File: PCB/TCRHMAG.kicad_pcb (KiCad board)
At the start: 2 copper layers, 45 x 36.1 mm, 12 parts, among them J1 CONN_BATTERY, J2 CONN_LED, J3 CONN_THERM, SW1 PWR_SW, U1 CH32V003FxPx, U2 L78L05_SOT89

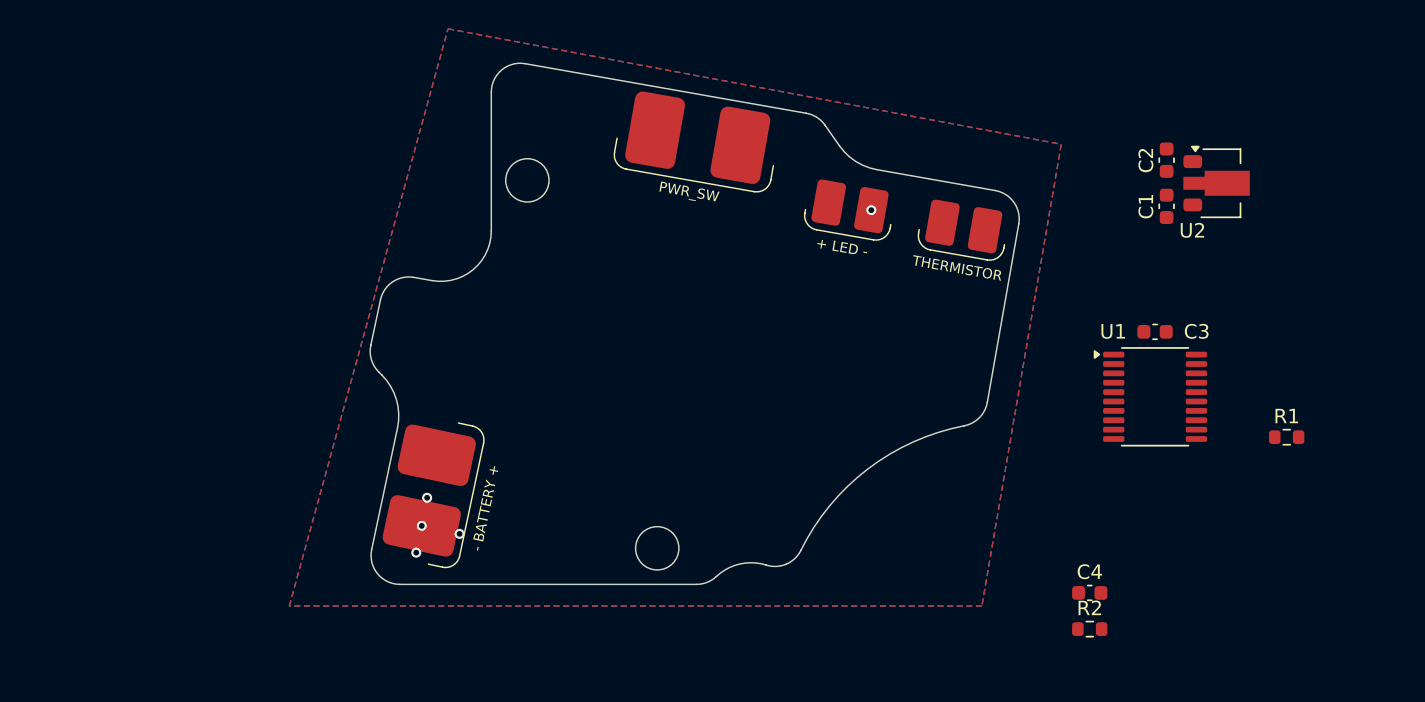
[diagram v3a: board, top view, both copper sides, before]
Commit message: Added High Current and MCU to PCB
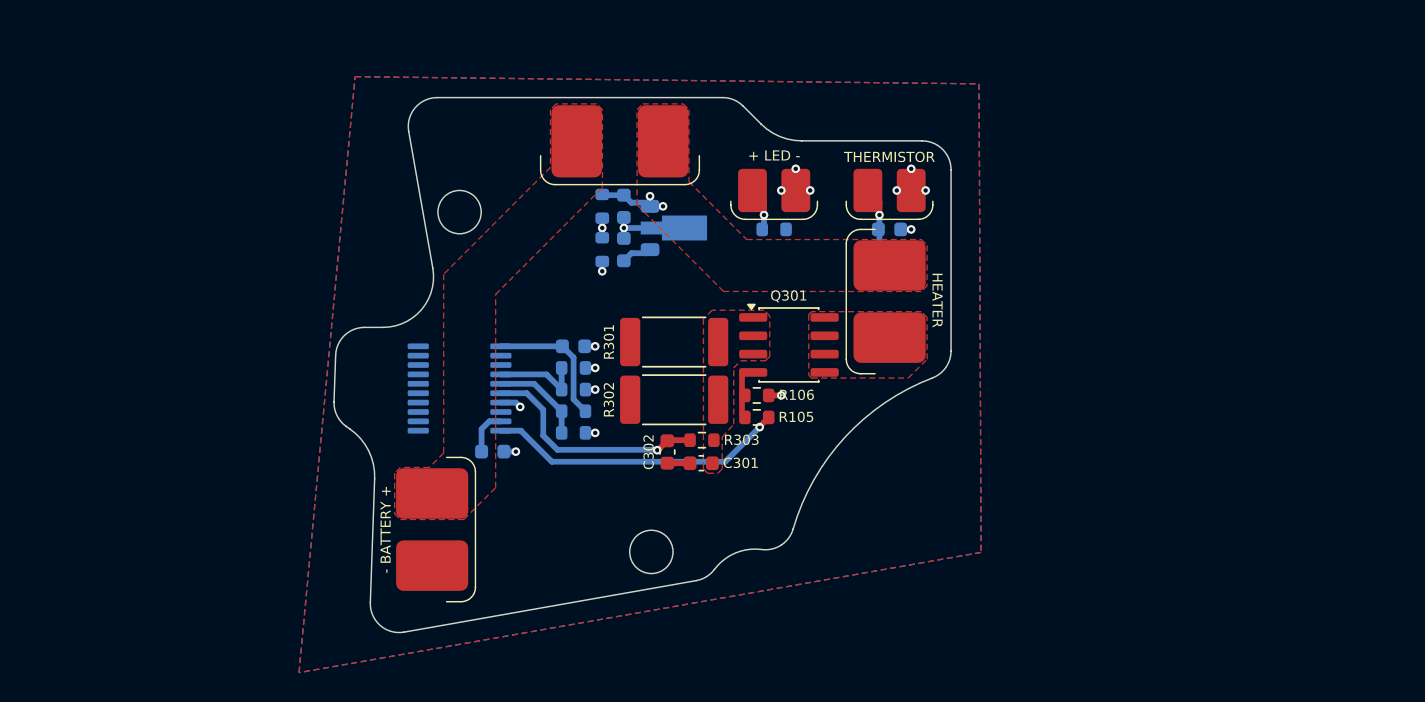
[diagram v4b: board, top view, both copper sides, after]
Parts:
- removed C1, C3: 100nF, Capacitor_SMD:C_0603_1608Metric
- removed C2: 10uF, Capacitor_SMD:C_0603_1608Metric
- removed C4: 1uF, Capacitor_SMD:C_0603_1608Metric
- removed R1: 330R, Resistor_SMD:R_0603_1608Metric
- removed R2: 4K7, Resistor_SMD:R_0603_1608Metric
- removed SW1: PWR_SW, TCRHMAG:U13SS_Switch
- removed U1: CH32V003FxPx, Package_SO:TSSOP-20_4.4x6.5mm_P0.65mm
- removed U2: L78L05_SOT89, Package_TO_SOT_SMD:SOT-89-3
- added C101: 100nF, Capacitor_SMD:C_0603_1608Metric, B.Cu at (82.7, 63.8)
- added C102: 10uF, Capacitor_SMD:C_0603_1608Metric, B.Cu at (82.7, 66.8)
- added C103: 1uF, Capacitor_SMD:C_0603_1608Metric, B.Cu at (101.1, 65.4)
- added C104: 100nF, Capacitor_SMD:C_0603_1608Metric, B.Cu at (73.6, 80.8)
- added C201: 100nF, Capacitor_SMD:C_0603_1608Metric, B.Cu at (79.2, 73.5)
- added C301: 100nF, Capacitor_SMD:C_0603_1608Metric, F.Cu at (88.0, 81.6)
- added C302: 100nF, Capacitor_SMD:C_0603_1608Metric, F.Cu at (85.7, 80.8)
- added J5: CONN_HEATER, TCRHMAG:Power_Conn, F.Cu at (101.1, 70.4)
- added Q301: Si4116DY, Package_SO:SOIC-8_3.9x4.9mm_P1.27mm, F.Cu at (94.1, 73.4)
- added R101: 33K, Resistor_SMD:R_0603_1608Metric, B.Cu at (81.2, 63.8)
- added R102: 8K2, Resistor_SMD:R_0603_1608Metric, B.Cu at (81.2, 66.8)
- added R103: 330R, Resistor_SMD:R_0603_1608Metric, B.Cu at (93.1, 65.4)
- added R104: 4K7, Resistor_SMD:R_0603_1608Metric, B.Cu at (101.1, 66.9)
- added R105: 10R, Resistor_SMD:R_0603_1608Metric, F.Cu at (91.9, 78.4)
- added R106: 33K, Resistor_SMD:R_0603_1608Metric, F.Cu at (91.9, 76.9)
- added R201: 2K2, Resistor_SMD:R_0603_1608Metric, B.Cu at (79.2, 79.5)
- added R202: 33K, Resistor_SMD:R_0603_1608Metric, B.Cu at (79.2, 78.0)
- added R203: 68K, Resistor_SMD:R_0603_1608Metric, B.Cu at (79.2, 75.0)
- added R204: 2K2, Resistor_SMD:R_0603_1608Metric, B.Cu at (79.2, 76.5)
- added R301: 0R075, Resistor_SMD:R_2512_6332Metric_Pad1.40x3.35mm_HandSolder, F.Cu at (86.2, 73.2)
- added R302: 0R075, Resistor_SMD:R_2512_6332Metric_Pad1.40x3.35mm_HandSolder, F.Cu at (86.2, 77.2)
- added R303: 33K, Resistor_SMD:R_0603_1608Metric, F.Cu at (88.1, 80.0)
- added SW101: PWR_SW, TCRHMAG:U13SS_Switch, F.Cu at (82.4, 59.3)
- added U101: L78L05_SOT89, Package_TO_SOT_SMD:SOT-89-3, B.Cu at (86.5, 65.3)
- added U102: CH32V003FxPx, Package_SO:TSSOP-20_4.4x6.5mm_P0.65mm, B.Cu at (71.3, 76.4)
- moved J3 5.71 mm to (101.1, 62.7), turned to 0 degrees
- moved J2 5.38 mm to (93.1, 62.7), turned to 0 degrees
- moved J1 2.71 mm to (69.4, 86.2), turned to 90 degrees
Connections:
- J1 pad 2: Net-(J1-Pin_2) -> /BATTERY_FILL
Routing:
- net /MCU_PWM_OUT: track 0.00 -> 20.8 mm, vias 0 -> 1
- net /MCU_OPAMP_CH1+: track 0.00 -> 16.1 mm, vias 0 -> 1
- net GND: track 0.00 -> 12.8 mm, vias 5 -> 15
- net /MCU_OPAMP_OUT: track 0.00 -> 9.43 mm
- net /MCU_OPAMP_CH1-: track 0.00 -> 6.50 mm
- net /MCU_OPAMP_CH2+: track 0.00 -> 6.15 mm
- net /PBUS_5V: track 0.00 -> 5.93 mm, vias 0 -> 1
- net /PBUS_BATT: track 0.00 -> 5.25 mm, vias 0 -> 2
- net /MCU_THERM_IN: track 0.00 -> 4.58 mm, vias 0 -> 1
- net Net-(Q301-G): track 0.00 -> 3.98 mm
- net Net-(J2-Pin_1): track 0.00 -> 3.08 mm, vias 0 -> 1
- net /MCU_BATT_VSENS: track 0.00 -> 1.55 mm, vias 0 -> 1
- added copper zone on F.Cu, net /BATTERY_FILL
- added copper zone on F.Cu, net /CSENSE_FILL
- added copper zone on F.Cu, net /HEATER_FILL
- added copper zone on F.Cu, net /PBUS_BATT
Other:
- board size 45 x 36.1 mm -> 42.8 x 37.1 mm
- board text added: "HEATER"

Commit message: Firmware Testing
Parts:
- added J6: CONN_PROG, TCRHMAG:Program_Conn, F.Cu at (64.9, 75.7)
- added R107: 4K7, Resistor_SMD:R_0603_1608Metric, F.Cu at (44.3, 89.9)
- added R108: 4K7, Resistor_SMD:R_0603_1608Metric, F.Cu at (44.3, 92.4)
- moved C104 0.21 mm to (73.8, 80.8)
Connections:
- net /MCU_OPAMP_OUT renamed /MCU_OPAMP_ADC
- U102 pad 2: unconnected-(U102-PD5-Pad2) -> /MCU_THERM_IN
- U102 pad 20: unconnected-(U102-PD3-Pad20) -> /MCU_LED_OUT
- U102 pad 3: unconnected-(U102-PD6-Pad3) -> /MCU_BATT_VSENS
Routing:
- net /PBUS_5V: track 5.93 -> 58.1 mm, vias 1 -> 4
- net /MCU_THERM_IN: track 4.58 -> 37.0 mm
- net /MCU_LED_OUT: track 0.00 -> 29.3 mm, vias 0 -> 2
- net /MCU_BATT_VSENS: track 1.55 -> 19.0 mm, vias 1 -> 0
- net /MCU_SWIO: track 0.00 -> 14.0 mm, vias 0 -> 1
- net /MCU_SCL: track 0.00 -> 11.0 mm
- net /MCU_SDA: track 0.00 -> 10.8 mm
- net unconnected-(U102-PC3-Pad13): track 0.00 -> 10.7 mm
- net unconnected-(U102-PC5-Pad15): track 0.00 -> 10.5 mm
- net unconnected-(U102-PC4-Pad14): track 0.00 -> 9.87 mm
- net GND: track 12.8 -> 13.2 mm, vias 15 -> 34
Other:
- board text added: "GND"
- board text added: "SWIO"
- board text added: "VCC"

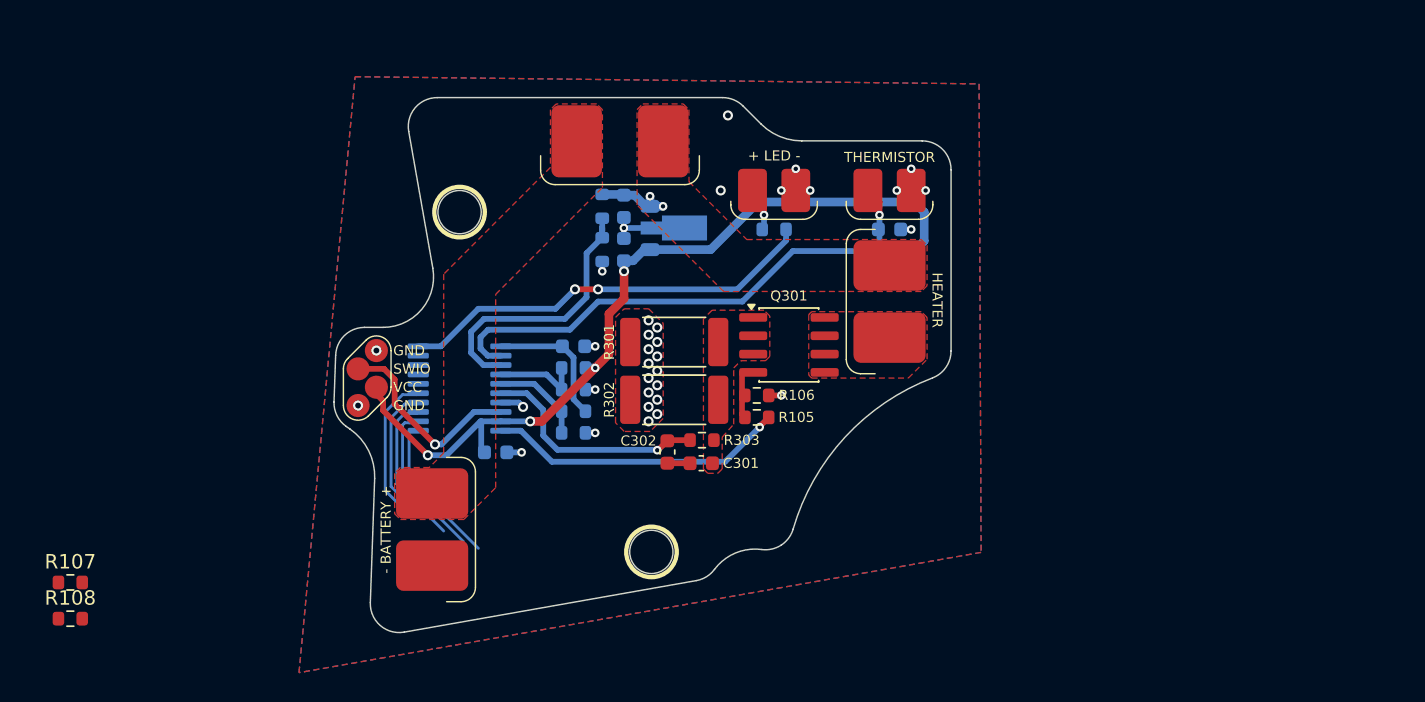
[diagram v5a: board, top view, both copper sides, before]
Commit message: Added temperature Linear Interpolation
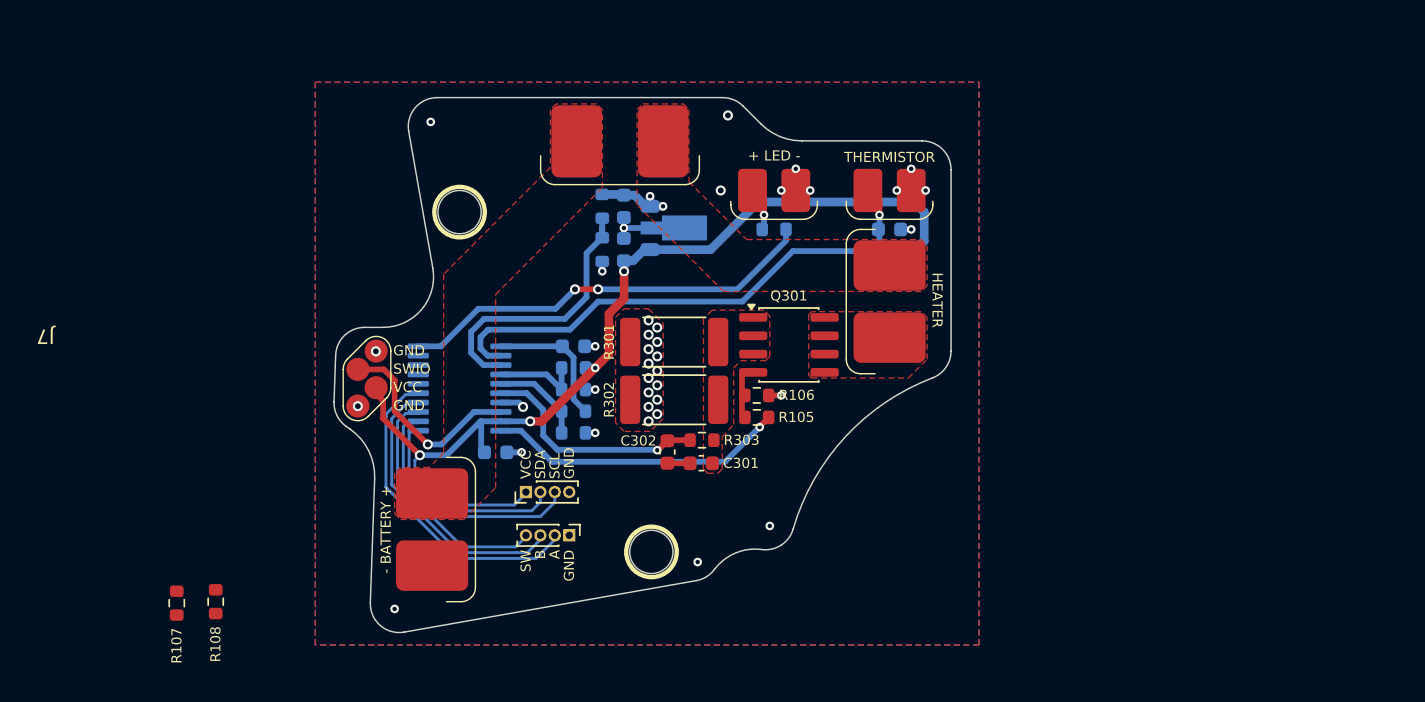
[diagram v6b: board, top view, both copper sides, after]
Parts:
- added J4: CONN_OLED, Connector_PinHeader_1.00mm:PinHeader_1x04_P1.00mm_Vertical, F.Cu at (75.9, 83.6)
- added J7: CONN_PROG, TCRHMAG:Program_Conn, F.Cu at (64.9, 75.7)
- J6: value CONN_PROG -> CONN_ENCODER; footprint TCRHMAG:Program_Conn -> Connector_PinHeader_1.00mm:PinHeader_1x04_P1.00mm_Vertical
- moved J6 17.7 mm to (78.9, 86.6), turned to -90 degrees
- moved R108 10.1 mm to (54.4, 91.2), turned to -90 degrees
- moved R107 7.51 mm to (51.7, 91.3), turned to -90 degrees
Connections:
- J6 pad 2: /PBUS_5V -> /MCU_ENC_A
- J6 pad 3: /MCU_SWIO -> /MCU_ENC_B
- J6 pad 4: GND -> /MCU_ENC_SW
- R107 pad 2: /MCU_SCL -> /MCU_SDA
- R108 pad 2: /MCU_SDA -> /MCU_SCL
- U102 pad 13: unconnected-(U102-PC3-Pad13) -> /MCU_ENC_SW
- U102 pad 14: unconnected-(U102-PC4-Pad14) -> /MCU_ENC_B
- U102 pad 15: unconnected-(U102-PC5-Pad15) -> /MCU_ENC_A
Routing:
- net /MCU_ENC_A: track 0.00 -> 22.5 mm
- net /MCU_ENC_B: track 0.00 -> 19.8 mm
- net /MCU_ENC_SW: track 0.00 -> 17.0 mm
- net /PBUS_5V: track 58.1 -> 68.8 mm
- net unconnected-(U102-PC3-Pad13): track 10.7 -> 0.00 mm
- net unconnected-(U102-PC5-Pad15): track 10.5 -> 0.00 mm
- net unconnected-(U102-PC4-Pad14): track 9.87 -> 0.00 mm
- net /MCU_SCL: track 11.0 -> 17.5 mm
- net /MCU_SDA: track 10.8 -> 14.8 mm
- net GND: vias 34 -> 38
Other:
- board text added: "A"
- board text added: "B"
- board text added: "SCL"
- board text added: "SDA"
- board text added: "SW"

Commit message: Final PCB
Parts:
- moved R107 31.3 mm to (81.8, 82.8), turned to 180 degrees
- moved R108 28.2 mm to (81.8, 84.4), turned to 180 degrees
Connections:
- net /MCU_PWM_OUT renamed /MCU_HEATER_OUT
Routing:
- net /PBUS_5V: track 68.8 -> 78.2 mm
- net /MCU_SDA: track 14.8 -> 19.8 mm
- net /MCU_SCL: track 17.5 -> 21.5 mm
- net GND: track 13.2 -> 13.7 mm, vias 38 -> 67

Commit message: Fixed SWIO Bug. MkII HW
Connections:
- U102 pad 18: unconnected-(U102-PD1-Pad18) -> /MCU_SWIO
- U102 pad 8: /MCU_SWIO -> unconnected-(U102-PD0-Pad8)
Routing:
- net GND: track 13.7 -> 25.0 mm, vias 67 -> 71
- net /MCU_SWIO: track 14.2 -> 4.31 mm
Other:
- board text added: "POWER SWITCH"
- board text added: "TCRHMAG Controller MkII 19 Mar 2026"
